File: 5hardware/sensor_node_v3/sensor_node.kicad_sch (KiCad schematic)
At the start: 21 parts, among them J3 Conn_01x29, SW2 SW_DIP_x04, SW3 SW_Push, SW4 SW_DIP_x04, SW5 RotaryEncoder, SW6 SW_Push, U1 MCP1700x-330xxTO, U7 CH32V003F4P6, U8 ESP32-WROOM-32D

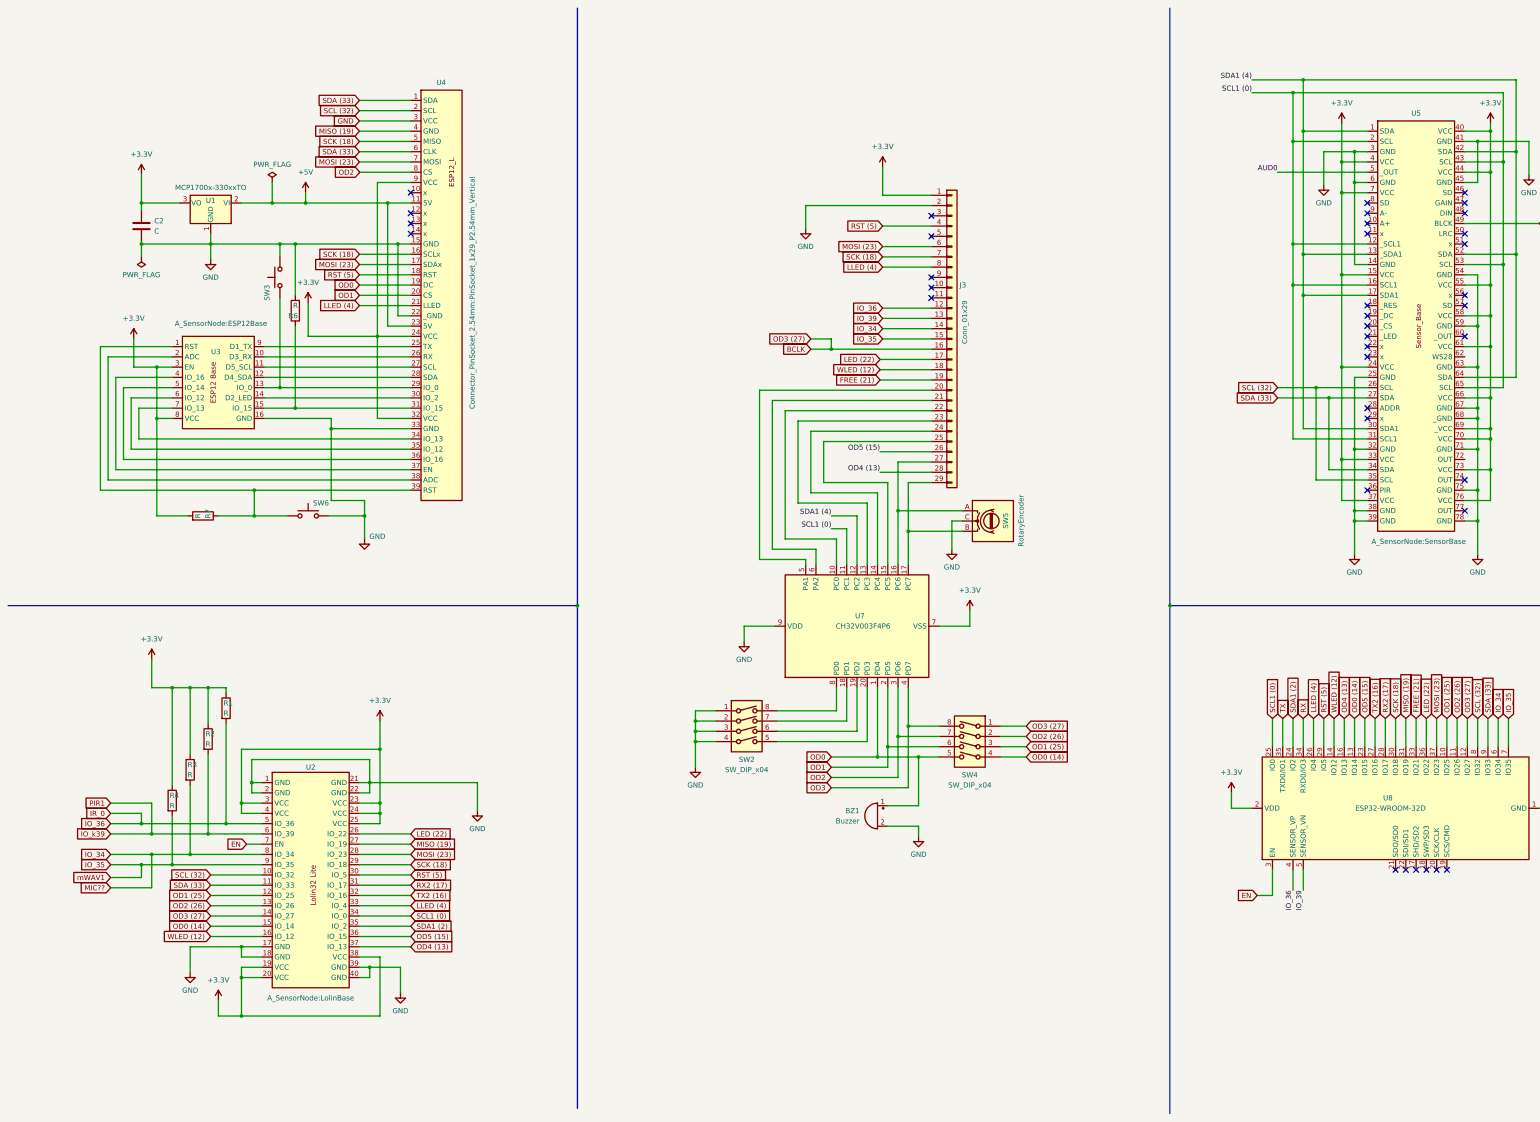
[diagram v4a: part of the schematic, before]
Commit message: added pcb design.
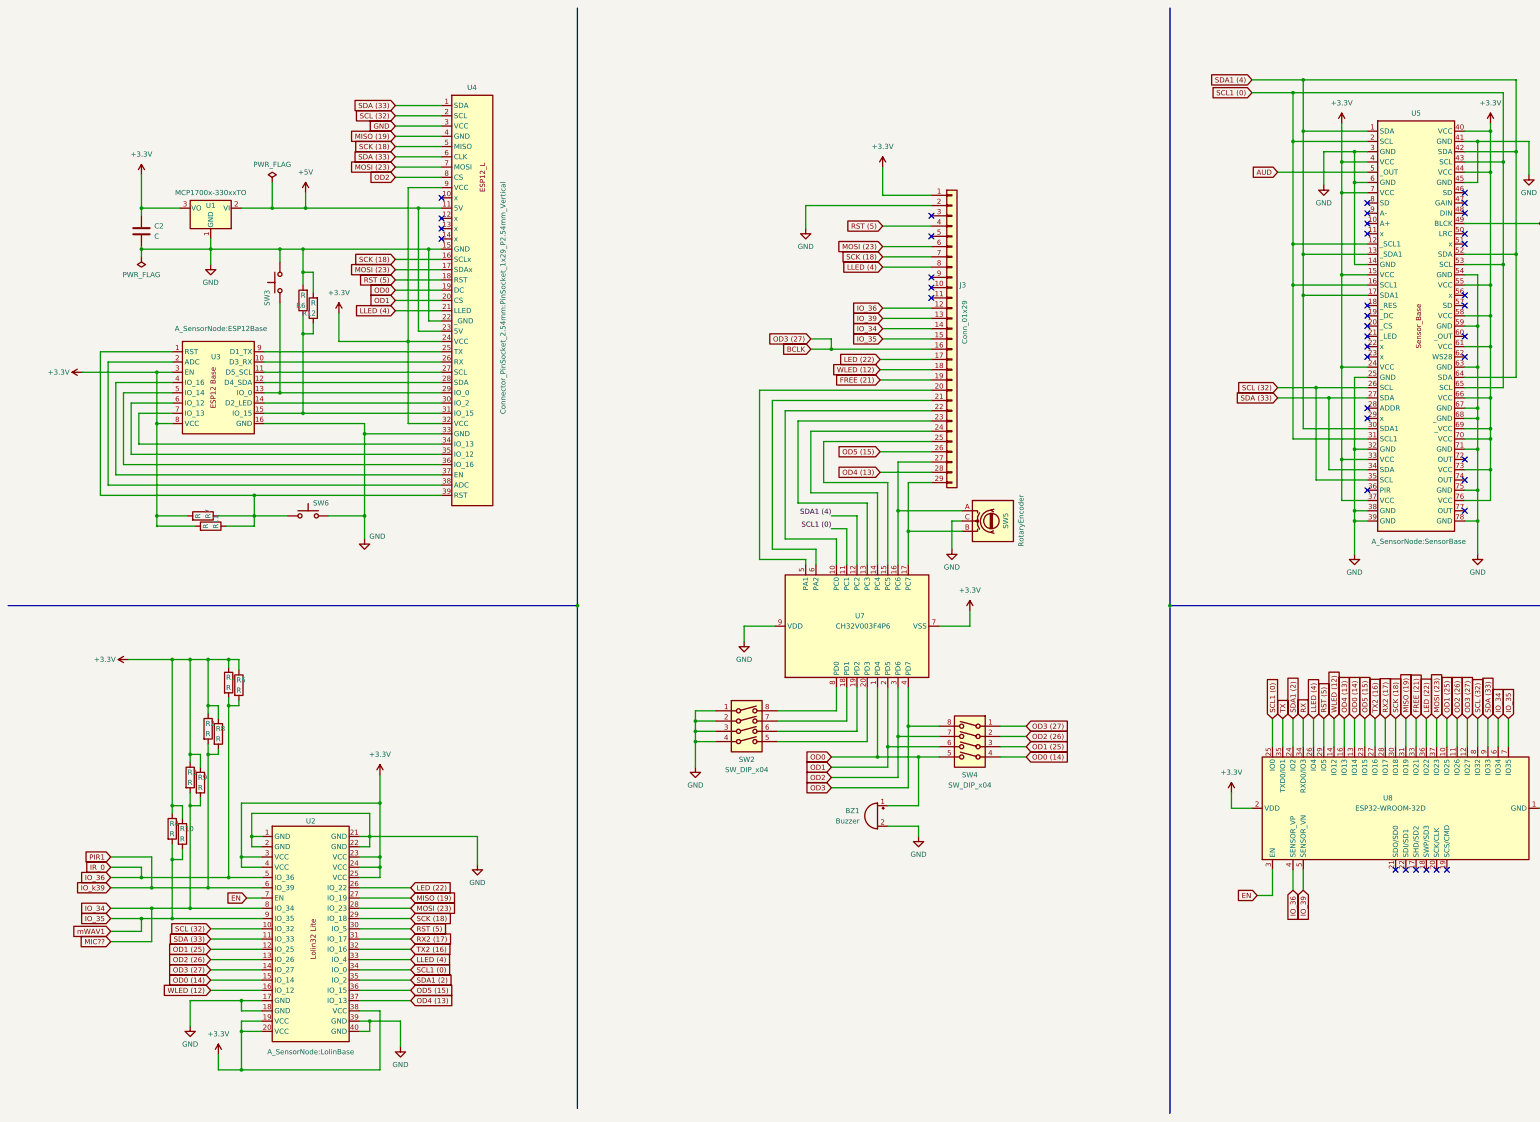
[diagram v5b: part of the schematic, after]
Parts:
- added R10, R11, R12, R5, R8, R9: R, Resistor_SMD:R_2512_6332Metric, symbol Device:R
- SW4: footprint Button_Switch_THT:SW_DIP_SPSTx04_Slide_6.7x11.72mm_W7.62mm_P2.54mm_LowProfile -> Button_Switch_SMD:SW_DIP_SPSTx04_Slide_6.7x11.72mm_W8.61mm_P2.54mm_LowProfile
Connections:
- net +3.3V: now also R10.1, R11.2, R5.1, R8.1, R9.1
- net GND: now also R12.2
- net IO_34: now also R9.2
- net IO_35: now also R10.2
- net IO_36: now also R5.2
- net IO_k39: now also R8.2
- net at R7.1, SW6.2, U3.1 (RST)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: now also R11.1
- net at R6.1, U3.15 (IO_15), U4.31 (IO_15): now also R12.1
- net AUD0 renamed AUD
- no-connect marks 38 -> 40
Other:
- moved on the sheet: C2, R1, R2, R3, R4, R6, SW3, U1, U2, U3, U4

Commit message: updating pcb design.
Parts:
- added J1: Conn_01x03, Connector_PinHeader_2.54mm:PinHeader_1x03_P2.54mm_Vertical, symbol Connector_Generic:Conn_01x03
- BZ1: footprint Buzzer_Beeper:Buzzer_12x9.5RM7.6 -> A_SensorNode:BuzzerSmall
- SW6: footprint Button_Switch_THT:SW_PUSH_6mm_H7.3mm -> Button_Switch_THT:SW_PUSH-12mm
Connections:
- net at J3.10 (Pin_10): now also J1.2 (Pin_2)
- net at J3.11 (Pin_11): now also J1.3 (Pin_3)
- net at J3.9 (Pin_9): now also J1.1 (Pin_1)
- no-connect marks 40 -> 37
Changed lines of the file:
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@@
   (no_connect (at 348.615 67.945))
   (no_connect (at 372.745 70.485))
-  (no_connect (at 240.665 81.28))
-  (no_connect (at 240.665 83.82))
   (no_connect (at 372.745 93.345))
   (no_connect (at 348.615 113.665))
@@
   (no_connect (at 363.22 225.425))
   (no_connect (at 348.615 111.125))
-  (no_connect (at 240.665 78.74))
   (no_connect (at 348.615 131.445))
   (no_connect (at 372.745 123.825))
@@
     (stroke (width 0) (type default) (color 255 0 0 1))
   )
+  (wire (pts (xy 237.49 81.28) (xy 240.665 81.28))
+    (stroke (width 0) (type default))
+  )
   (wire (pts (xy 382.27 75.565) (xy 372.745 75.565))
     (stroke (width 0) (type default) (color 194 194 194 1))
@@
     (stroke (width 0) (type default))
   )
-  (wire (pts (xy 215.9 137.795) (xy 222.25 137.795))
+  (wire (pts (xy 218.44 137.795) (xy 222.25 137.795))
     (stroke (width 0) (type default) (color 0 0 0 1))
   )
@@
     (stroke (width 0) (type default) (color 194 0 194 1))
   )
+  (wire (pts (xy 237.49 78.74) (xy 240.665 78.74))
+    (stroke (width 0) (type default))
+  )
   (wire (pts (xy 379.095 80.645) (xy 379.095 88.265))
     (stroke (width 0) (type default) (color 255 0 0 1))
@@
     (stroke (width 0) (type default) (color 194 0 194 1))
   )
+  (wire (pts (xy 237.49 83.82) (xy 240.665 83.82))
+    (stroke (width 0) (type default))
+  )
   (wire (pts (xy 107.95 84.455) (xy 119.38 84.455))
     (stroke (width 0) (type default) (color 255 153 0 1))
@@
     (stroke (width 0) (type default))
   )
-  (wire (pts (xy 215.9 140.97) (xy 219.71 140.97))
+  (wire (pts (xy 218.44 140.97) (xy 219.71 140.97))
     (stroke (width 0) (type default) (color 194 194 194 1))
   )
@@
     (stroke (width 0) (type default) (color 255 0 0 1))
   )
-  (label "SDA1 (4)" (at 215.9 137.795 180) (fields_autoplaced)
-    (effects (font (size 1.27 1.27)) (justify right bottom))
-  )
-  (label "SCL1 (0)" (at 215.9 140.97 180) (fields_autoplaced)
-    (effects (font (size 1.27 1.27) (color 194 194 194 1)) (justify right bottom))
-  )
   (global_label "MOSI (23)" (shape input) (at 107.95 76.835 180) (fields_autoplaced)
     (effects (font (size 1.27 1.27)) (justify right))
@@
     )
   )
+  (global_label "SCL1 (0)" (shape input) (at 218.44 140.97 180) (fields_autoplaced)
+    (effects (font (size 1.27 1.27)) (justify right))
+    (property "Intersheetrefs" "${INTERSHEET_REFS}" (at 206.8672 140.97 0)
+      (effects (font (size 1.27 1.27)) (justify right) hide)
+    )
+  )
   (global_label "FREE (21)" (shape input) (at 360.68 187.96 90) (fields_autoplaced)
     (effects (font (size 1.27 1.27)) (justify left))
@@
     )
   )
+  (global_label "SDA1 (4)" (shape input) (at 218.44 137.795 180) (fields_autoplaced)
+    (effects (font (size 1.27 1.27)) (justify right))
+    (property "Intersheetrefs" "${INTERSHEET_REFS}" (at 206.8067 137.795 0)
+      (effects (font (size 1.27 1.27)) (justify right) hide)
+    )
+  )
   (global_label "SCK (18)" (shape input) (at 107.95 46.355 180) (fields_autoplaced)
     (effects (font (size 1.27 1.27)) (justify right))
@@
     )
   )
+  (symbol (lib_id "Connector_Generic:Conn_01x03") (at 232.41 81.28 0) (mirror y) (unit 1)
+    (in_bom yes) (on_board yes) (dnp no) (fields_autoplaced)
+    (property "Reference" "J1" (at 232.41 72.39 0)
+      (effects (font (size 1.27 1.27)))
+    )
+    (property "Value" "Conn_01x03" (at 232.41 74.93 0)
+      (effects (font (size 1.27 1.27)))
+    )
+    (property "Footprint" "Connector_PinHeader_2.54mm:PinHeader_1x03_P2.54mm_Vertical" (at 232.41 81.28 0)
+      (effects (font (size 1.27 1.27)) hide)
+    )
+    (property "Datasheet" "~" (at 232.41 81.28 0)
+      (effects (font (size 1.27 1.27)) hide)
+    )
+    (pin "1")
+    (pin "2")
+    (pin "3")
+    (instances
+      (project "sensor_node"
+        (path "/af3a10dd-48b4-4881-8409-82af1b899ed6"
+          (reference "J1") (unit 1)
+        )
+      )
+    )
+  )
   (symbol (lib_id "power:+3.3V") (at 45.085 53.34 0) (unit 1)
     (in_bom yes) (on_board yes) (dnp no) (fields_autoplaced)
@@
       (effects (font (size 1.27 1.27)) hide)
     )
-    (property "Footprint" "Button_Switch_THT:SW_PUSH_6mm_H7.3mm" (at 86.36 132.715 0)
+    (property "Footprint" "Button_Switch_THT:SW_PUSH-12mm" (at 86.36 132.715 0)
       (effects (font (size 1.27 1.27)) hide)
     )
@@
       (effects (font (size 1.27 1.27)) (justify left))
     )
-    (property "Footprint" "Buzzer_Beeper:Buzzer_12x9.5RM7.6" (at 227.965 209.55 90)
+    (property "Footprint" "A_SensorNode:BuzzerSmall" (at 227.965 209.55 90)
       (effects (font (size 1.27 1.27)) hide)
     )

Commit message: updated schematic. ESP32-C3 support.
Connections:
- net FREE (21) is gone; now on net AUD (21): J3.19 (Pin_19), U8.33 (IO21)
- net IO_k39 is gone; now on net IO_39: R2.2, R8.2, U2.6 (IO_39)
- net RX is gone; now on net RX (3): U8.34 (RXD0/IO3)
- net TX is gone; now on net TX (1): U8.35 (TXD0/IO1)
- net +3.3V: now also U4.3 (VCC)
- net BCLK: now also J1.3 (Pin_3)
- net GND: now also U4.4 (GND); no longer U4.3 (VCC)
- net IO_34: now also J1.2 (Pin_2), U5.48 (DIN)
- net MISO (19): no longer U4.4 (GND)
- net OD0: now also J3.5 (Pin_5)
- net OD1: now also J3.3 (Pin_3)
- net OD2: now also J3.9 (Pin_9)
- net SCK (18): now also U4.6 (CLK); no longer U4.5 (MISO)
- net SDA (33): no longer U4.6 (CLK)
- net WLED (12): now also U5.62 (WS28)
- net at J1.1 (Pin_1): no longer J3.9 (Pin_9)
- net RX (3): now reaches J3.10 (Pin_10)
- net RX (3): no longer J1.2 (Pin_2)
- net TX (1): now reaches J3.11 (Pin_11)
- net TX (1): no longer J1.3 (Pin_3)
- net AUD (21): now reaches U5.10 (A+)
- net AUD: no longer names the net of U5.5 (_OUT)
- new net MISO (23): U4.5 (MISO)
- no-connect marks 37 -> 34
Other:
- moved on the sheet: J1

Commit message: updating pcb design.
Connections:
- net EN is gone; now on net +3.3V: U2.7 (EN), U8.3 (EN)
- net MISO (23) is gone; now on net MISO (19): U4.5 (MISO)
- net OD3 is gone; now on net BCLK: SW4.8, U7.4 (PD7)
- net SDA1 (4) is gone; now on net SDA1 (2): U5.1 (SDA), U5.13 (_SDA1), U5.17 (SDA1), U5.30 (SDA1), U5.42 (SDA), U5.52 (SDA), U5.64 (SDA), U7.12 (PC2)
- net +3.3V: now also U5.19 (_VCC)
- net BCLK: no longer SW4.1, U2.14 (IO_27), U8.12 (IO27)
- net GND: now also U5.18 (_GND), U5.23 (_GND), U5.72 (GND), U5.77 (GND), U5.9 (A-); no longer U5.71 (GND), U5.78 (GND)
- net IO_35: now also U5.74 (OUT)
- net IO_36: now also U5.78 (OUT)
- net IO_39: now also U5.36 (PIR)
- net RX2 (17): now also U5.56 (x)
- net SCL1 (0): now also U5.22 (_SCL1)
- net SDA1 (2): now also U5.21 (_SDA1)
- net TX2 (16): now also U5.51 (x)
- net WLED (12): now also U5.71 (OUT)
- new net OD3 (27): SW4.1, U2.14 (IO_27), U8.12 (IO27)
- no-connect marks 34 -> 22
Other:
- moved on the sheet: J1
